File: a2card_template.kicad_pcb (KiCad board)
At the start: 2 copper layers, 158.8 x 76.4 mm, 6 parts, among them U1 74LS373, U10 PLCCZ80, U14 74LS367, U16 74LS367, U17 74LS367

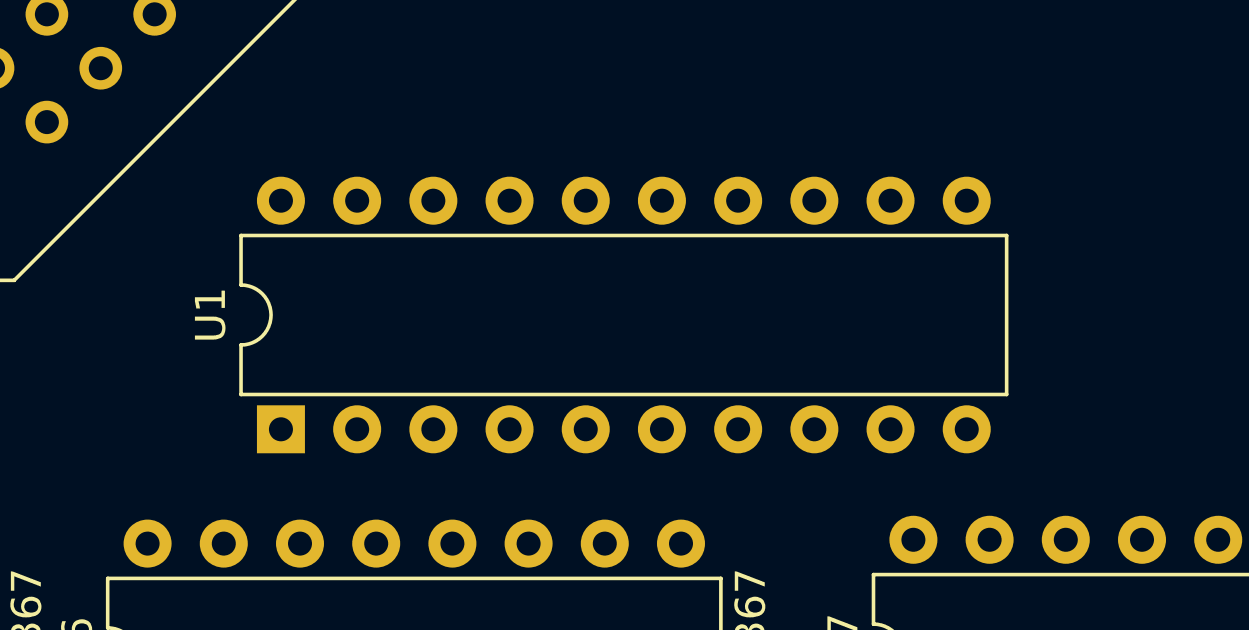
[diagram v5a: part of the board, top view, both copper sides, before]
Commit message: Fix reference for U15
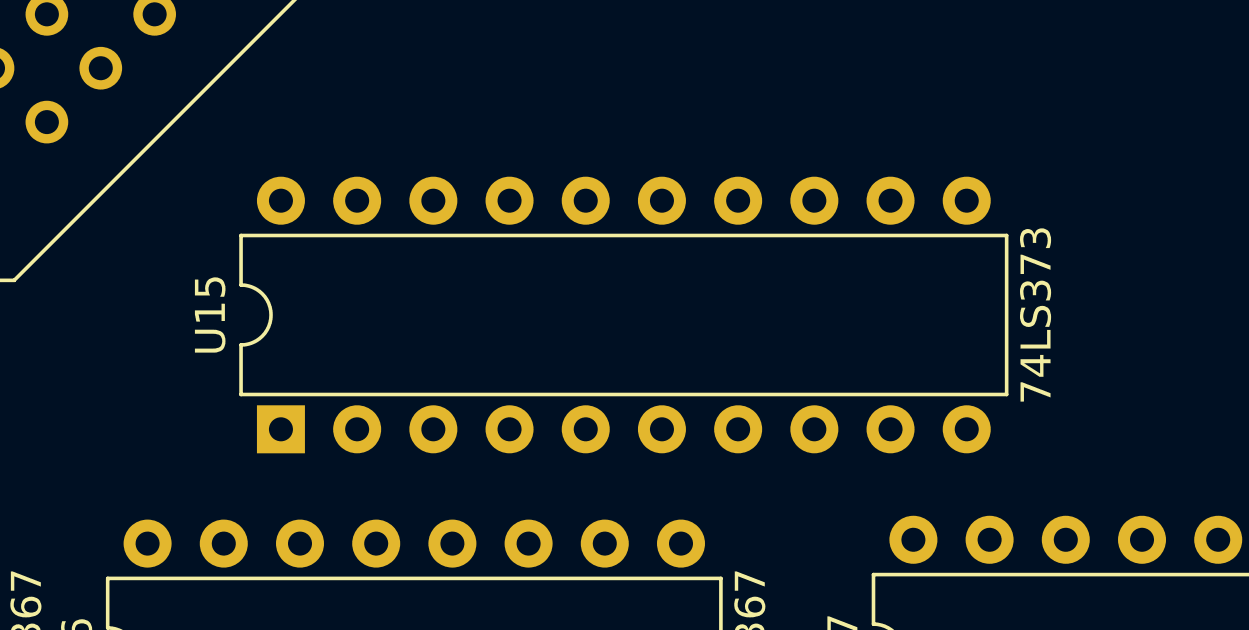
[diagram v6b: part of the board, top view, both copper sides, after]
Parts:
- renumbered U1 to U15
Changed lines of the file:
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@@
   )
   (setup
-    (last_trace_width 0.5)
+    (last_trace_width 0.25)
     (user_trace_width 0.5)
     (user_trace_width 1)
@@
     (descr "20-lead though-hole mounted DIP package, row spacing 7.62 mm (300 mils)")
     (tags "THT DIP DIL PDIP 2.54mm 7.62mm 300mil")
-    (fp_text reference U1 (at 3.81 -2.33 90) (layer F.SilkS)
+    (fp_text reference U15 (at 3.81 -2.33 90) (layer F.SilkS)
       (effects (font (size 1 1) (thickness 0.15)))
     )
-    (fp_text value 74LS373 (at 3.81 25.19 90) (layer F.Fab)
+    (fp_text value 74LS373 (at 3.81 25.19 90) (layer F.SilkS)
       (effects (font (size 1 1) (thickness 0.15)))
     )

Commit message: Configuration DIP
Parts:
- added RN9: 10kΩ, Resistor_THT:R_Array_SIP5, F.Cu at (185.2, 79.8)
- added S1: SW_DIP_x04, Button_Switch_THT:SW_DIP_SPSTx04_Slide_9.78x12.34mm_W7.62mm_P2.54mm, F.Cu at (199.5, 80.8)
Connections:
- BUS1 pad 29: Net-(BUS1-Pad29) -> /~NMI
- BUS1 pad 30: Net-(BUS1-Pad30) -> /~IRQ
- U10 pad 18: Net-(U10-Pad18) -> /~Z80_IRQ
- U10 pad 19: Net-(U10-Pad19) -> /~Z80_NMI

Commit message: Popping more junk
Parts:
- added R13: 10kΩ, Resistor_THT:R_Array_SIP9, F.Cu at (89.4, 77.5)
- added U9: 74LS367, Package_DIP:DIP-16_W7.62mm, F.Cu at (113.6, 77.4)
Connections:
- net Net-(BUS1-Pad36) renamed /7M
- BUS1 pad 23: Net-(BUS1-Pad23) -> /INT_IN_OUT
- BUS1 pad 27: Net-(BUS1-Pad27) -> /DMA_IN
- BUS1 pad 28: Net-(BUS1-Pad28) -> /INT_IN_OUT
- RN9 pad 3: Net-(RN9-Pad3) -> /DMA_IN
- S1 pad 2: Net-(S1-Pad2) -> /~BUSRQ
- S1 pad 7: Net-(S1-Pad7) -> /DMA_IN
- U10 pad 29: Net-(U10-Pad29) -> /~BUSRQ
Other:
- board text added: "26"
- board text added: "50"
